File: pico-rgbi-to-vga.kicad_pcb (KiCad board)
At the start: 2 copper layers, 68.8 x 59 mm, 25 parts, among them J1 SDS-80J, J2 DB15_Female_HighDensity, J3 USB-B1HSB6, SW1 SW_Push, SW2 Intensity Select, U1 Pico

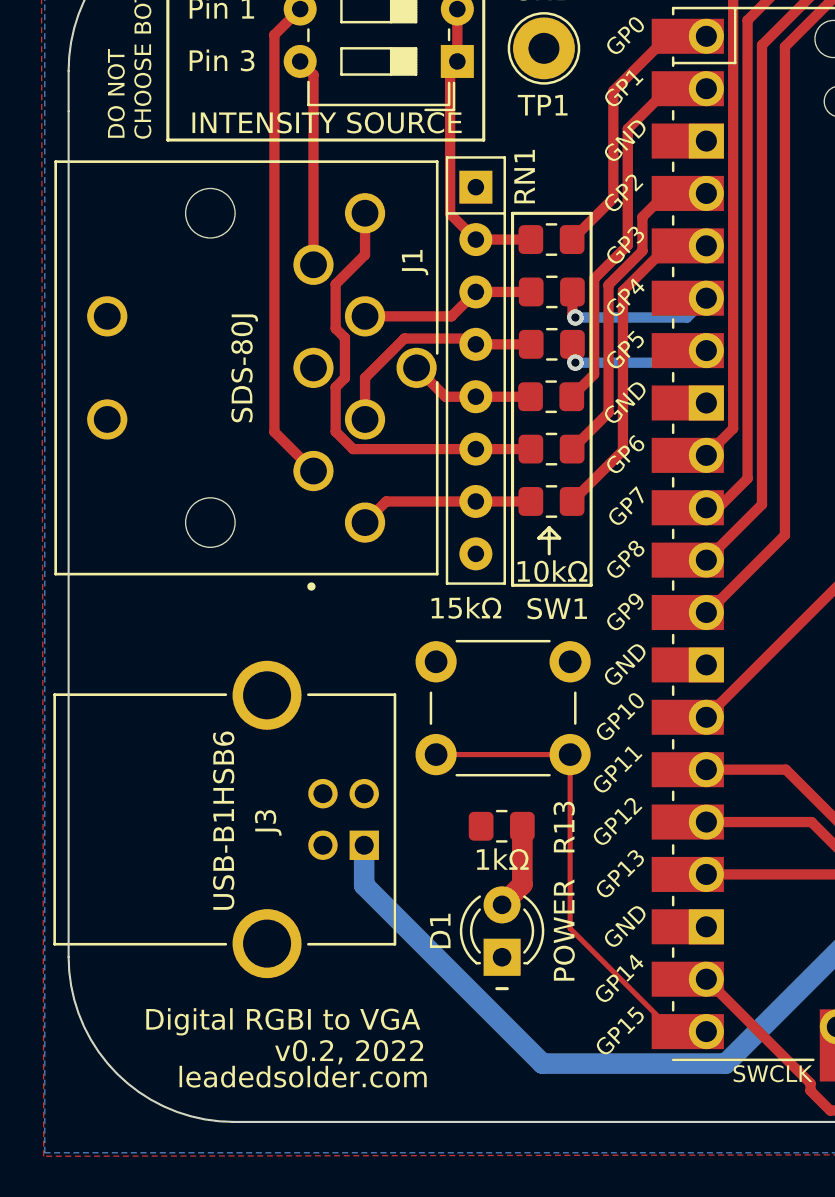
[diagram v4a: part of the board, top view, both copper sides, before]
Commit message: Rewired to be IBGRHV
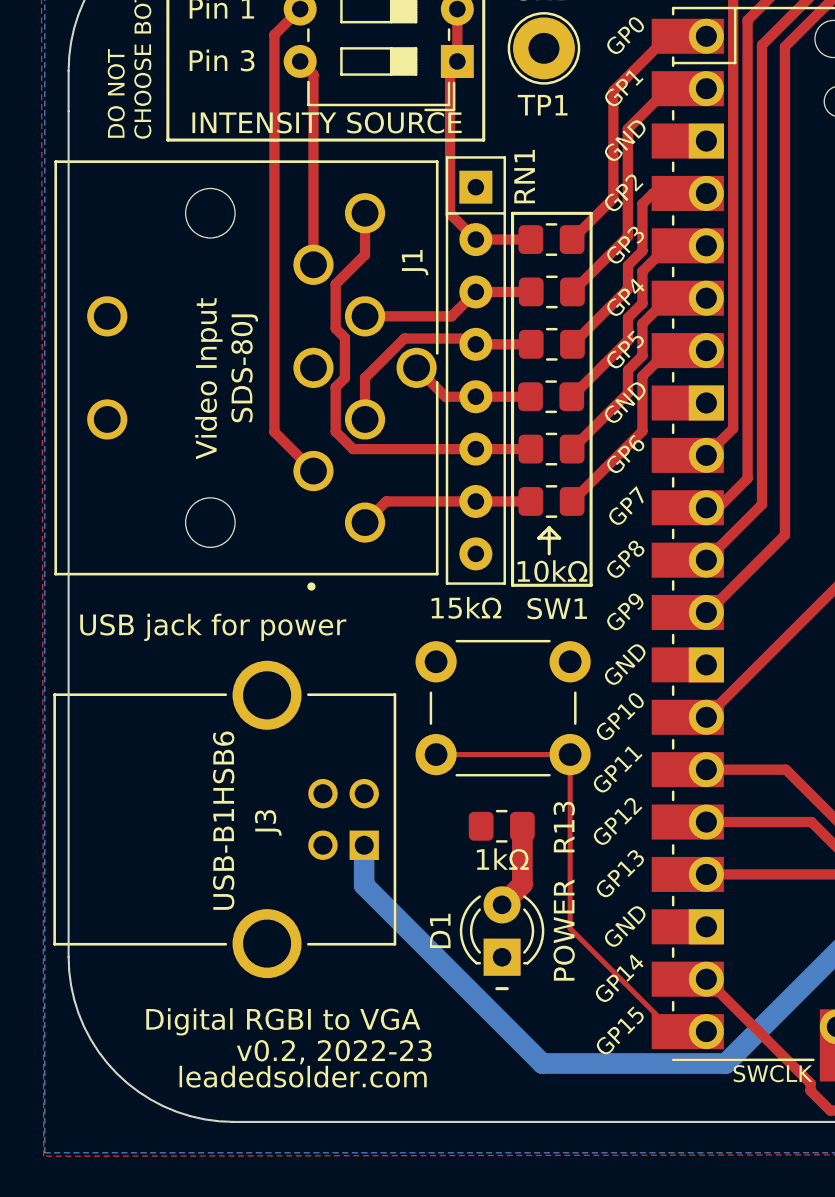
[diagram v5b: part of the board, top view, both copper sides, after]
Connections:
- R1 pad 1: /RED_3v3 -> /HSYNC_3v3
- R2 pad 1: /GREEN_3v3 -> /VSYNC_3v3
- R3 pad 1: /BLUE_3v3 -> /RED_3v3
- R4 pad 1: /HSYNC_3v3 -> /GREEN_3v3
- R5 pad 1: /VSYNC_3v3 -> /BLUE_3v3
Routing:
- net /BLUE_3v3: track 18.7 -> 13.6 mm
- net /RED_3v3: track 16.2 -> 11.1 mm
- net /GREEN_3v3: track 16.2 -> 11.5 mm
- net /HSYNC_3v3: track 7.54 -> 11.1 mm, vias 1 -> 0
- net /VSYNC_3v3: track 8.04 -> 11.1 mm, vias 1 -> 0
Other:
- board text added: "USB jack for power"
- board text added: "Video Input"
- board text added: "v0.2, 2022-23"
- board text removed: "v0.2, 2022"
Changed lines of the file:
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@@
       (stroke (width 0.1) (type solid)) (layer "F.Fab"))
     (pad "1" smd roundrect (at -1 0 180) (size 1.2 1.4) (layers "F.Cu" "F.Paste" "F.Mask") (roundrect_rratio 0.2083333333)
-      (net 43 "/BLUE_3v3") (pintype "passive"))
+      (net 41 "/RED_3v3") (pintype "passive"))
     (pad "2" smd roundrect (at 1 0 180) (size 1.2 1.4) (layers "F.Cu" "F.Paste" "F.Mask") (roundrect_rratio 0.2083333333)
       (net 7 "/BLUE_IN") (pintype "passive"))
@@
       (stroke (width 0.1) (type solid)) (layer "F.Fab"))
     (pad "1" smd roundrect (at -1 0 180) (size 1.2 1.4) (layers "F.Cu" "F.Paste" "F.Mask") (roundrect_rratio 0.2083333333)
-      (net 44 "/HSYNC_3v3") (pintype "passive"))
+      (net 42 "/GREEN_3v3") (pintype "passive"))
     (pad "2" smd roundrect (at 1 0 180) (size 1.2 1.4) (layers "F.Cu" "F.Paste" "F.Mask") (roundrect_rratio 0.2083333333)
       (net 3 "/HSYNC_IN") (pintype "passive"))
@@
       (stroke (width 0.1) (type solid)) (layer "F.Fab"))
     (pad "1" smd roundrect (at -1 0 180) (size 1.2 1.4) (layers "F.Cu" "F.Paste" "F.Mask") (roundrect_rratio 0.2083333333)
-      (net 45 "/VSYNC_3v3") (pintype "passive"))
+      (net 43 "/BLUE_3v3") (pintype "passive"))
     (pad "2" smd roundrect (at 1 0 180) (size 1.2 1.4) (layers "F.Cu" "F.Paste" "F.Mask") (roundrect_rratio 0.2083333333)
       (net 4 "/VSYNC_IN") (pintype "passive"))
@@
       (stroke (width 0.1) (type solid)) (layer "F.Fab"))
     (pad "1" smd roundrect (at -1 0 180) (size 1.2 1.4) (layers "F.Cu" "F.Paste" "F.Mask") (roundrect_rratio 0.2083333333)
-      (net 42 "/GREEN_3v3") (pintype "passive"))
+      (net 45 "/VSYNC_3v3") (pintype "passive"))
     (pad "2" smd roundrect (at 1 0 180) (size 1.2 1.4) (layers "F.Cu" "F.Paste" "F.Mask") (roundrect_rratio 0.2083333333)
       (net 6 "/GREEN_IN") (pintype "passive"))
@@
       (stroke (width 0.1) (type solid)) (layer "F.Fab"))
     (pad "1" smd roundrect (at -1 0 180) (size 1.2 1.4) (layers "F.Cu" "F.Paste" "F.Mask") (roundrect_rratio 0.2083333333)
-      (net 41 "/RED_3v3") (pintype "passive"))
+      (net 44 "/HSYNC_3v3") (pintype "passive"))
     (pad "2" smd roundrect (at 1 0 180) (size 1.2 1.4) (layers "F.Cu" "F.Paste" "F.Mask") (roundrect_rratio 0.2083333333)
       (net 5 "/RED_IN") (pintype "passive"))
@@
     (effects (font (size 1 1) (thickness 0.15)))
   )
-  (gr_text "v0.2, 2022" (at 114.808 116.586) (layer "F.SilkS")
-    (effects (font (size 1 1) (thickness 0.15)))
+  (gr_text "USB jack for power" (at 101.6 96.52) (layer "F.SilkS")
+    (effects (font (size 1 1) (thickness 0.15)) (justify left bottom))
+  )
+  (gr_text "Video Input" (at 108.458 87.884 90) (layer "F.SilkS")
+    (effects (font (size 1 1) (thickness 0.15)) (justify left bottom))
+  )
+  (gr_text "v0.2, 2022-23" (at 118.872 116.586) (layer "F.SilkS")
+    (effects (font (size 1 1) (thickness 0.15)) (justify right))
   )
   (gr_text "DO NOT\nCHOOSE BOTH" (at 104.14 72.39 90) (layer "F.SilkS")
@@
   (segment (start 143.51 106.68) (end 133.020489 117.169511) (width 1) (layer "B.Cu") (net 38))
   (segment (start 133.020489 117.169511) (end 124.130489 117.169511) (width 1) (layer "B.Cu") (net 38))
-  (segment (start 128.036002 79.703998) (end 128.036002 87.450998) (width 0.5) (layer "F.Cu") (net 41))
-  (segment (start 128.036002 87.450998) (end 125.571 89.916) (width 0.5) (layer "F.Cu") (net 41))
+  (segment (start 128.280499 82.110501) (end 125.555 84.836) (width 0.5) (layer "F.Cu") (net 41))
+  (segment (start 130.22 77.52) (end 128.98 78.76) (width 0.5) (layer "F.Cu") (net 41))
+  (segment (start 128.98 80.310756) (end 128.280499 81.010257) (width 0.5) (layer "F.Cu") (net 41))
+  (segment (start 128.280499 81.010257) (end 128.280499 82.110501) (width 0.5) (layer "F.Cu") (net 41))
   (segment (start 132.08 77.52) (end 130.22 77.52) (width 0.5) (layer "F.Cu") (net 41))
-  (segment (start 130.22 77.52) (end 128.036002 79.703998) (width 0.5) (layer "F.Cu") (net 41))
-  (segment (start 127.336501 85.610499) (end 127.336501 79.414255) (width 0.5) (layer "F.Cu") (net 42))
-  (segment (start 128.98 77.770756) (end 128.98 76.125) (width 0.5) (layer "F.Cu") (net 42))
-  (segment (start 128.98 76.125) (end 130.125 74.98) (width 0.5) (layer "F.Cu") (net 42))
-  (segment (start 125.571 87.376) (end 127.336501 85.610499) (width 0.5) (layer "F.Cu") (net 42))
-  (segment (start 130.125 74.98) (end 132.08 74.98) (width 0.5) (layer "F.Cu") (net 42))
-  (segment (start 127.336501 79.414255) (end 128.98 77.770756) (width 0.5) (layer "F.Cu") (net 42))
-  (segment (start 128.27 77.491512) (end 126.637 79.124512) (width 0.5) (layer "F.Cu") (net 43))
-  (segment (start 128.27 71.85) (end 128.27 77.491512) (width 0.5) (layer "F.Cu") (net 43))
-  (segment (start 126.637 83.754) (end 125.555 84.836) (width 0.5) (layer "F.Cu") (net 43))
-  (segment (start 126.637 79.124512) (end 126.637 83.754) (width 0.5) (layer "F.Cu") (net 43))
+  (segment (start 128.98 78.76) (end 128.98 80.310756) (width 0.5) (layer "F.Cu") (net 41))
+  (segment (start 129.49 74.98) (end 132.08 74.98) (width 0.5) (layer "F.Cu") (net 42))
+  (segment (start 128.280499 78.470257) (end 128.98 77.770756) (width 0.5) (layer "F.Cu") (net 42))
+  (segment (start 128.280499 79.602501) (end 128.280499 78.470257) (width 0.5) (layer "F.Cu") (net 42))
+  (segment (start 128.98 77.770756) (end 128.98 75.49) (width 0.5) (layer "F.Cu") (net 42))
+  (segment (start 128.98 75.49) (end 129.49 74.98) (width 0.5) (layer "F.Cu") (net 42))
+  (segment (start 125.587 82.296) (end 128.280499 79.602501) (width 0.5) (layer "F.Cu") (net 42))
+  (segment (start 130.22 69.9) (end 128.27 71.85) (width 0.5) (layer "F.Cu") (net 43))
+  (segment (start 128.27 71.85) (end 128.27 77.073) (width 0.5) (layer "F.Cu") (net 43))
   (segment (start 132.08 69.9) (end 130.22 69.9) (width 0.5) (layer "F.Cu") (net 43))
-  (segment (start 130.22 69.9) (end 128.27 71.85) (width 0.5) (layer "F.Cu") (net 43))
-  (segment (start 125.587 83.042) (end 125.73 83.185) (width 0.5) (layer "F.Cu") (net 44))
-  (segment (start 125.587 82.296) (end 125.587 83.042) (width 0.5) (layer "F.Cu") (net 44))
-  (via (at 125.73 83.185) (size 0.8) (drill 0.4) (layers "F.Cu" "B.Cu") (net 44))
-  (segment (start 125.73 83.185) (end 131.495 83.185) (width 0.5) (layer "B.Cu") (net 44))
-  (segment (start 131.495 83.185) (end 132.08 82.6) (width 0.5) (layer "B.Cu") (net 44))
-  (segment (start 125.587 79.756) (end 125.587 80.8535) (width 0.5) (layer "F.Cu") (net 45))
-  (segment (start 125.587 80.8535) (end 125.73 80.9965) (width 0.5) (layer "F.Cu") (net 45))
-  (via (at 125.73 80.9965) (size 0.8) (drill 0.4) (layers "F.Cu" "B.Cu") (net 45))
-  (segment (start 125.73 80.9965) (end 131.1435 80.9965) (width 0.5) (layer "B.Cu") (net 45))
-  (segment (start 131.1435 80.9965) (end 132.08 80.06) (width 0.5) (layer "B.Cu") (net 45))
+  (segment (start 128.27 77.073) (end 125.587 79.756) (width 0.5) (layer "F.Cu") (net 43))
+  (segment (start 128.98 83.84) (end 128.98 86.507) (width 0.5) (layer "F.Cu") (net 44))
+  (segment (start 130.22 82.6) (end 128.98 83.84) (width 0.5) (layer "F.Cu") (net 44))
+  (segment (start 128.98 86.507) (end 125.571 89.916) (width 0.5) (layer "F.Cu") (net 44))
+  (segment (start 132.08 82.6) (end 130.22 82.6) (width 0.5) (layer "F.Cu") (net 44))
+  (segment (start 128.280499 83.550257) (end 128.280499 84.666501) (width 0.5) (layer "F.Cu") (net 45))
+  (segment (start 132.08 80.06) (end 130.22 80.06) (width 0.5) (layer "F.Cu") (net 45))
+  (segment (start 130.22 80.06) (end 128.98 81.3) (width 0.5) (layer "F.Cu") (net 45))
+  (segment (start 128.280499 84.666501) (end 125.571 87.376) (width 0.5) (layer "F.Cu") (net 45))
+  (segment (start 128.98 81.3) (end 128.98 82.850756) (width 0.5) (layer "F.Cu") (net 45))
+  (segment (start 128.98 82.850756) (end 128.280499 83.550257) (width 0.5) (layer "F.Cu") (net 45))
   (segment (start 130.220978 67.36) (end 132.08 67.36) (width 0.5) (layer "F.Cu") (net 46))
   (segment (start 125.571 77.216) (end 127.570499 75.216501) (width 0.5) (layer "F.Cu") (net 46))

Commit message: Doubts about DIN8 pinout
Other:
- board text added: "VGA female output"
